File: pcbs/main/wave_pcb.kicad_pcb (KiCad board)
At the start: 2 copper layers, 114.5 x 95.5 mm, 28 parts

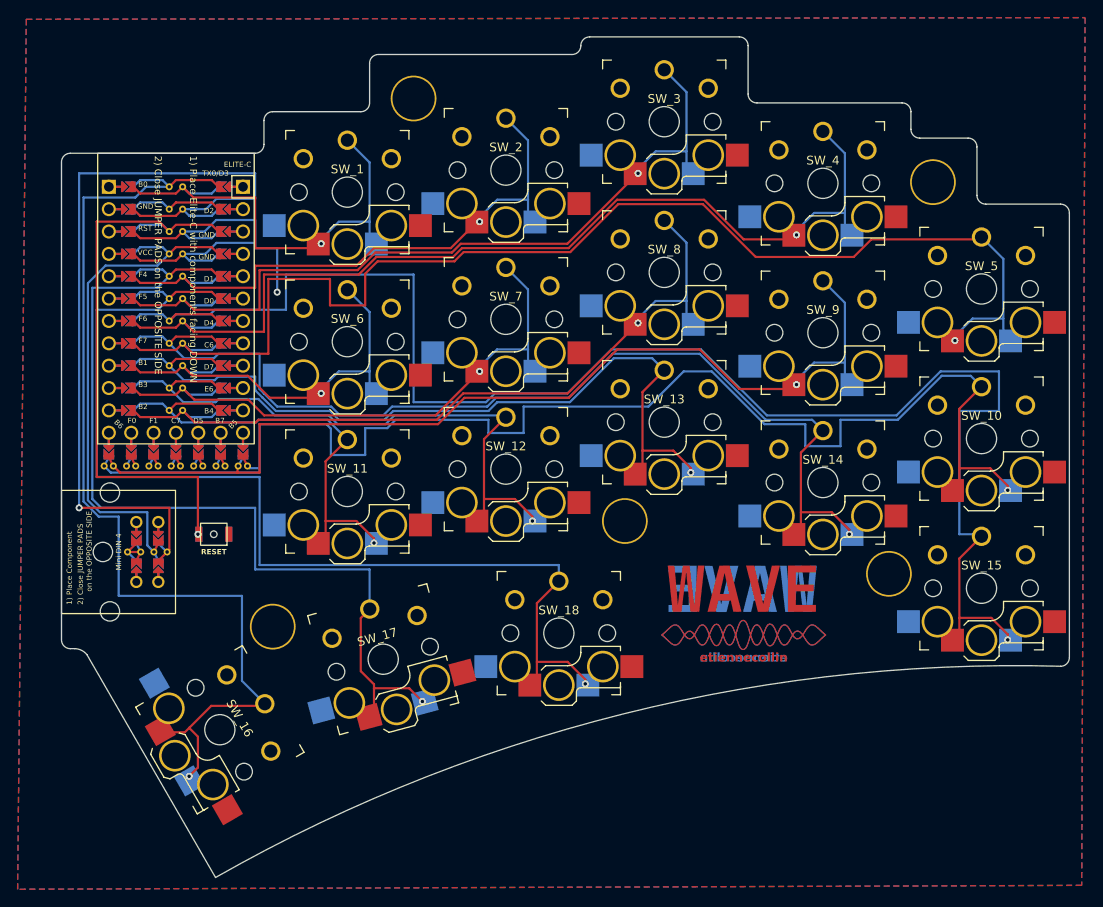
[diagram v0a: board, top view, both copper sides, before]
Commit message: Fixed spacing of PCB edges
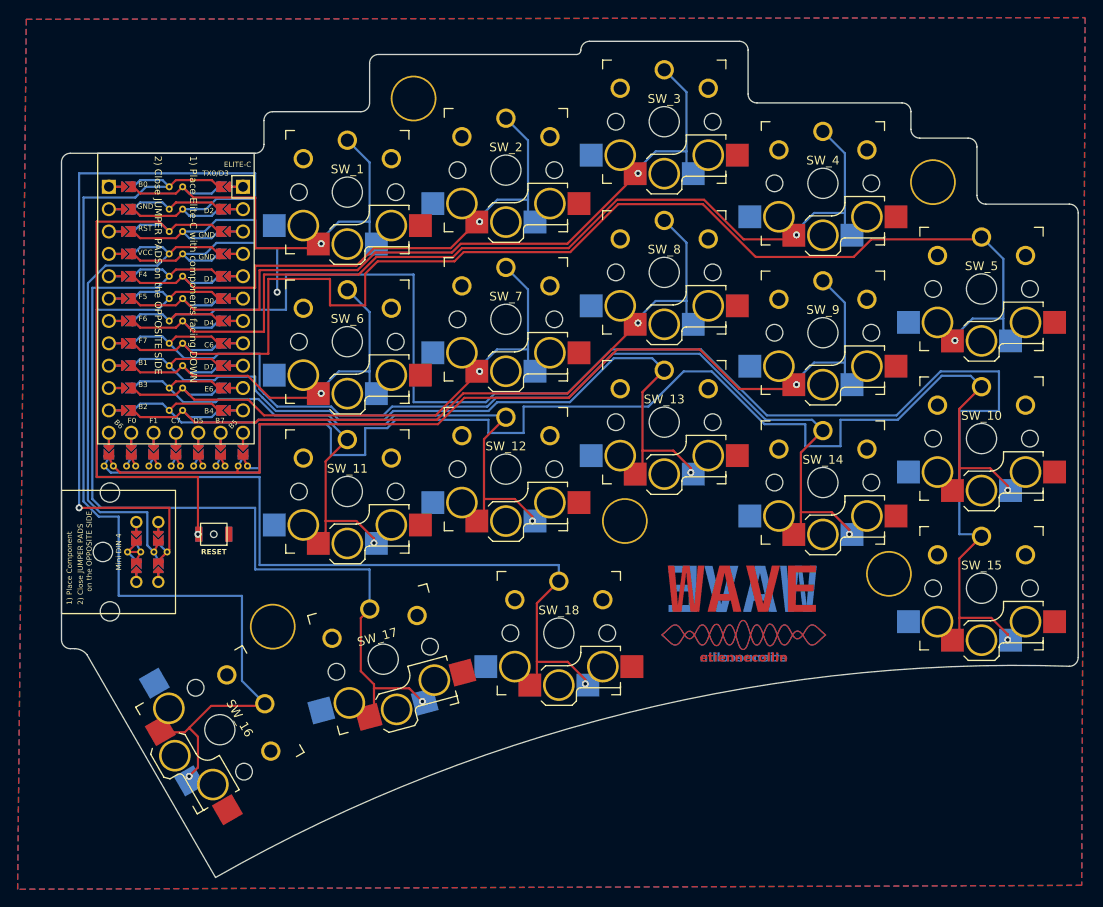
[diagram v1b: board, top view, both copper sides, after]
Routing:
- net Switch14: track 106.6 -> 105.5 mm
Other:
- board size 114.5 x 95.5 mm -> 115.5 x 95 mm
